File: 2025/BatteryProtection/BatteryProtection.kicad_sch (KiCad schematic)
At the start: 47 parts, among them J1 Conn_01x02_Socket, J2 Conn_01x02_Pin, J3 Conn_01x02_Pin, Q1 IXTA140P05T, Q10 BC847, Q11 BC847, Q12 BC847, Q2 BC847, Q3 BC847, Q4 BC847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

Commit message: Made a complete PCB design
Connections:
- net GPIO: now also J1.1 (Pin_1); no longer J3.1 (Pin_1)
- net VOUT: now also J3.1 (Pin_1); no longer J1.1 (Pin_1)
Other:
- moved on the sheet: J1
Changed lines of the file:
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@@
 	(wire
 		(pts
-			(xy 238.76 57.15) (xy 241.3 57.15)
-		)
-		(stroke
-			(width 0)
-			(type default)
-		)
-	)
-	(wire
-		(pts
 			(xy 39.37 175.26) (xy 41.91 175.26)
 		)
@@
 	(wire
 		(pts
-			(xy 257.81 90.17) (xy 262.89 90.17)
+			(xy 251.46 59.69) (xy 255.27 59.69)
 		)
 		(stroke
@@
 	(wire
 		(pts
-			(xy 238.76 59.69) (xy 241.3 59.69)
+			(xy 265.43 135.89) (xy 267.97 135.89)
 		)
 		(stroke
@@
 	(wire
 		(pts
-			(xy 265.43 135.89) (xy 267.97 135.89)
+			(xy 251.46 148.59) (xy 251.46 149.86)
 		)
 		(stroke
@@
 	(wire
 		(pts
-			(xy 251.46 148.59) (xy 251.46 149.86)
+			(xy 251.46 57.15) (xy 255.27 57.15)
 		)
 		(stroke
@@
 	(wire
 		(pts
-			(xy 238.76 62.23) (xy 238.76 59.69)
+			(xy 251.46 62.23) (xy 251.46 59.69)
 		)
 		(stroke
@@
 	(wire
 		(pts
-			(xy 260.35 92.71) (xy 257.81 92.71)
+			(xy 264.16 92.71) (xy 257.81 92.71)
 		)
 		(stroke
@@
 	(wire
 		(pts
-			(xy 260.35 95.25) (xy 260.35 92.71)
+			(xy 264.16 95.25) (xy 264.16 92.71)
 		)
 		(stroke
@@
 	(wire
 		(pts
+			(xy 251.46 53.34) (xy 251.46 57.15)
+		)
+		(stroke
+			(width 0)
+			(type default)
+		)
+	)
+	(wire
+		(pts
 			(xy 85.09 134.62) (xy 86.36 134.62)
 		)
@@
 	(wire
 		(pts
+			(xy 264.16 90.17) (xy 264.16 87.63)
+		)
+		(stroke
+			(width 0)
+			(type default)
+		)
+	)
+	(wire
+		(pts
 			(xy 110.49 64.77) (xy 116.84 64.77)
 		)
@@
 	(wire
 		(pts
-			(xy 238.76 54.61) (xy 238.76 57.15)
-		)
-		(stroke
-			(width 0)
-			(type default)
-		)
-	)
-	(wire
-		(pts
 			(xy 85.09 97.79) (xy 85.09 105.41)
 		)
@@
 	(wire
 		(pts
+			(xy 257.81 90.17) (xy 264.16 90.17)
+		)
+		(stroke
+			(width 0)
+			(type default)
+		)
+	)
+	(wire
+		(pts
 			(xy 124.46 167.64) (xy 124.46 189.23)
 		)
@@
 	(global_label "GPIO"
 		(shape input)
-		(at 262.89 90.17 0)
+		(at 251.46 53.34 180)
 		(fields_autoplaced yes)
 		(effects
@@
 				(size 1.27 1.27)
 			)
-			(justify left)
+			(justify right)
 		)
 		(property "Intersheetrefs" "${INTERSHEET_REFS}"
-			(at 270.3505 90.17 0)
+			(at 243.9995 53.34 0)
 			(effects
 				(font
 					(size 1.27 1.27)
 				)
-				(justify left)
+				(justify right)
 				(hide yes)
 			)
@@
 	(symbol
 		(lib_id "power:GND")
-		(at 238.76 62.23 0)
+		(at 251.46 62.23 0)
 		(unit 1)
 		(exclude_from_sim no)
@@
 		(fields_autoplaced yes)
 		(property "Reference" "#PWR027"
-			(at 238.76 68.58 0)
+			(at 251.46 68.58 0)
 			(effects
 				(font
@@
 		)
 		(property "Value" "GND"
-			(at 238.76 67.31 0)
+			(at 251.46 67.31 0)
 			(effects
 				(font
@@
 		)
 		(property "Footprint" ""
-			(at 238.76 62.23 0)
+			(at 251.46 62.23 0)
 			(effects
 				(font
@@
 		)
 		(property "Datasheet" ""
-			(at 238.76 62.23 0)
+			(at 251.46 62.23 0)
 			(effects
 				(font
@@
 		)
 		(property "Description" "Power symbol creates a global label with name \"GND\" , ground"
-			(at 238.76 62.23 0)
+			(at 251.46 62.23 0)
 			(effects
 				(font
@@
 	(symbol
 		(lib_id "power:GND")
-		(at 260.35 95.25 0)
+		(at 264.16 95.25 0)
 		(unit 1)
 		(exclude_from_sim no)
@@
 		(fields_autoplaced yes)
 		(property "Reference" "#PWR032"
-			(at 260.35 101.6 0)
+			(at 264.16 101.6 0)
 			(effects
 				(font
@@
 		)
 		(property "Value" "GND"
-			(at 260.35 100.33 0)
+			(at 264.16 100.33 0)
 			(effects
 				(font
@@
 		)
 		(property "Footprint" ""
-			(at 260.35 95.25 0)
+			(at 264.16 95.25 0)
 			(effects
 				(font
@@
 		)
 		(property "Datasheet" ""
-			(at 260.35 95.25 0)
+			(at 264.16 95.25 0)
 			(effects
 				(font
@@
 		)
 		(property "Description" "Power symbol creates a global label with name \"GND\" , ground"
-			(at 260.35 95.25 0)
+			(at 264.16 95.25 0)
 			(effects
 				(font
@@
 	(symbol
 		(lib_id "Connector:Conn_01x02_Socket")
-		(at 246.38 57.15 0)
+		(at 260.35 57.15 0)
 		(unit 1)
 		(exclude_from_sim no)
@@
 		(fields_autoplaced yes)
 		(property "Reference" "J1"
-			(at 247.65 57.1499 0)
+			(at 261.62 57.1499 0)
 			(effects
 				(font
@@
 		)
 		(property "Value" "Conn_01x02_Socket"
-			(at 247.65 59.6899 0)
+			(at 261.62 59.6899 0)
 			(effects
 				(font
@@
 		)
 		(property "Footprint" "Connector_JST:JST_XH_B2B-XH-A_1x02_P2.50mm_Vertical"
-			(at 246.38 57.15 0)
+			(at 260.35 57.15 0)
 			(effects
 				(font
@@
 		)
 		(property "Datasheet" "~"
-			(at 246.38 57.15 0)
+			(at 260.35 57.15 0)
 			(effects
 				(font
@@
 		)
 		(property "Description" "Generic connector, single row, 01x02, script generated"
-			(at 246.38 57.15 0)
+			(at 260.35 57.15 0)
 			(effects
 				(font
@@
 	(symbol
 		(lib_id "power:+3.3V")
-		(at 238.76 54.61 0)
+		(at 264.16 87.63 0)
 		(unit 1)
 		(exclude_from_sim no)
@@
 		(dnp no)
 		(property "Reference" "#PWR030"
-			(at 238.76 58.42 0)
+			(at 264.16 91.44 0)
 			(effects
 				(font
@@
 		)
 		(property "Value" "VOUT"
-			(at 238.76 50.8 0)
+			(at 264.16 83.82 0)
 			(effects
 				(font
@@
 		)
 		(property "Footprint" ""
-			(at 238.76 54.61 0)
+			(at 264.16 87.63 0)
 			(effects
 				(font
@@
 		)
 		(property "Datasheet" ""
-			(at 238.76 54.61 0)
+			(at 264.16 87.63 0)
 			(effects
 				(font
@@
 		)
 		(property "Description" "Power symbol creates a global label with name \"+3.3V\""
-			(at 238.76 54.61 0)
+			(at 264.16 87.63 0)
 			(effects
 				(font

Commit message: more work on PCB
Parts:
- added D1: LED, LED_SMD:LED_0805_2012Metric, symbol Device:LED
- added R26: 2.2k, Resistor_SMD:R_0603_1608Metric_Pad0.98x0.95mm_HandSolder, symbol Device:R_US
- added TP1: GPIO, TestPoint:TestPoint_Pad_D1.5mm, symbol Connector:TestPoint
- added TP2, TP7: Vout, TestPoint:TestPoint_Pad_D1.5mm, symbol Connector:TestPoint
- added TP3: Vin, TestPoint:TestPoint_Pad_D1.5mm, symbol Connector:TestPoint
- added TP4: U1 Out, TestPoint:TestPoint_Pad_D1.5mm, symbol Connector:TestPoint
- added TP5: U2 Out, TestPoint:TestPoint_Pad_D1.5mm, symbol Connector:TestPoint
- added TP6: Kill, TestPoint:TestPoint_Pad_D1.5mm, symbol Connector:TestPoint
- added TP8: Pmos In, TestPoint:TestPoint_Pad_D1.5mm, symbol Connector:TestPoint
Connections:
- net GND: now also R26.1
- net GPIO: now also TP1.1
- net VOUT: now also TP2.1
- net Vs: now also TP3.1
- net at R6.1, U2.1: now also TP5.1
- net at Q9.3 (C), R17.1, R18.1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: now also TP7.1
- net at Q1.1 (G), Q12.3 (C), R9.1: now also TP8.1
- net at Q8.3 (C), R13.1, R7.1: now also D1.2 (A), TP6.1
- net at R5.2, U1.1: now also TP4.1
- new net: D1.1 (K), R26.2

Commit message: DID the voltage protection PCB
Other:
- note removed: "Change transistors to this one"
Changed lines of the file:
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@@
-		)
-	)
-	(text "Change transistors to this one"
-		(exclude_from_sim no)
-		(at 182.88 144.78 0)
-		(effects
-			(font
-				(size 2.54 2.54)
-				(thickness 0.508)
-				(bold yes)
-			)
 		)
 	)

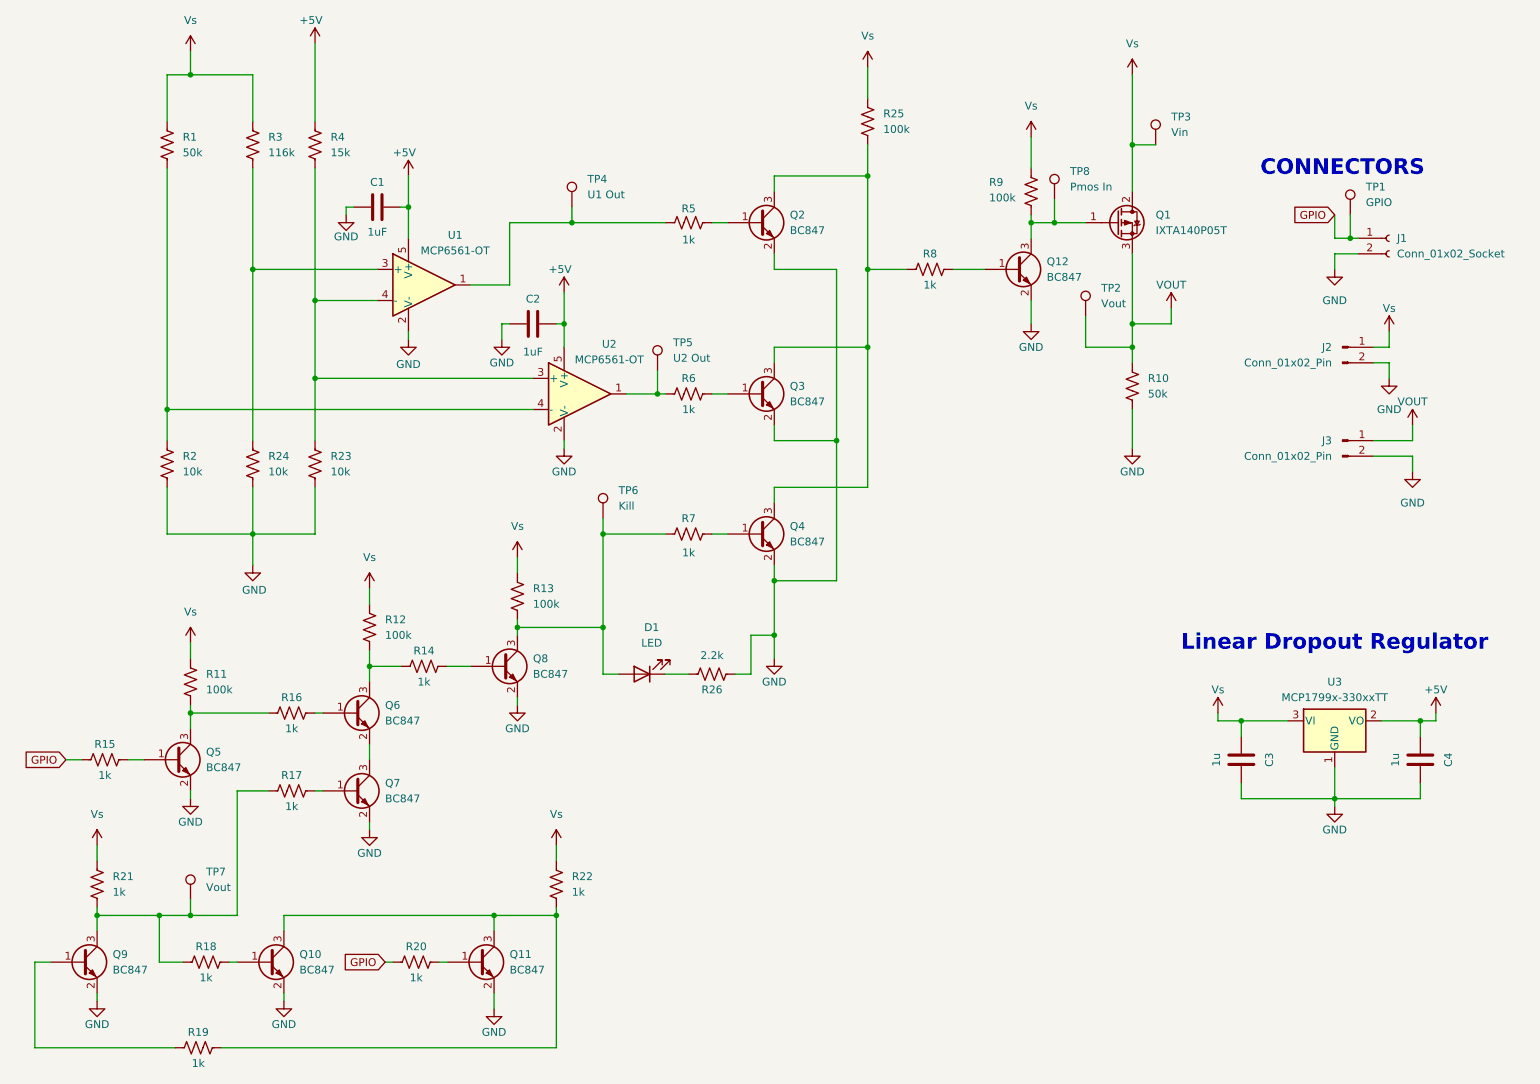
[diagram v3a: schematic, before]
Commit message: Added Switch to Bat Protect Board
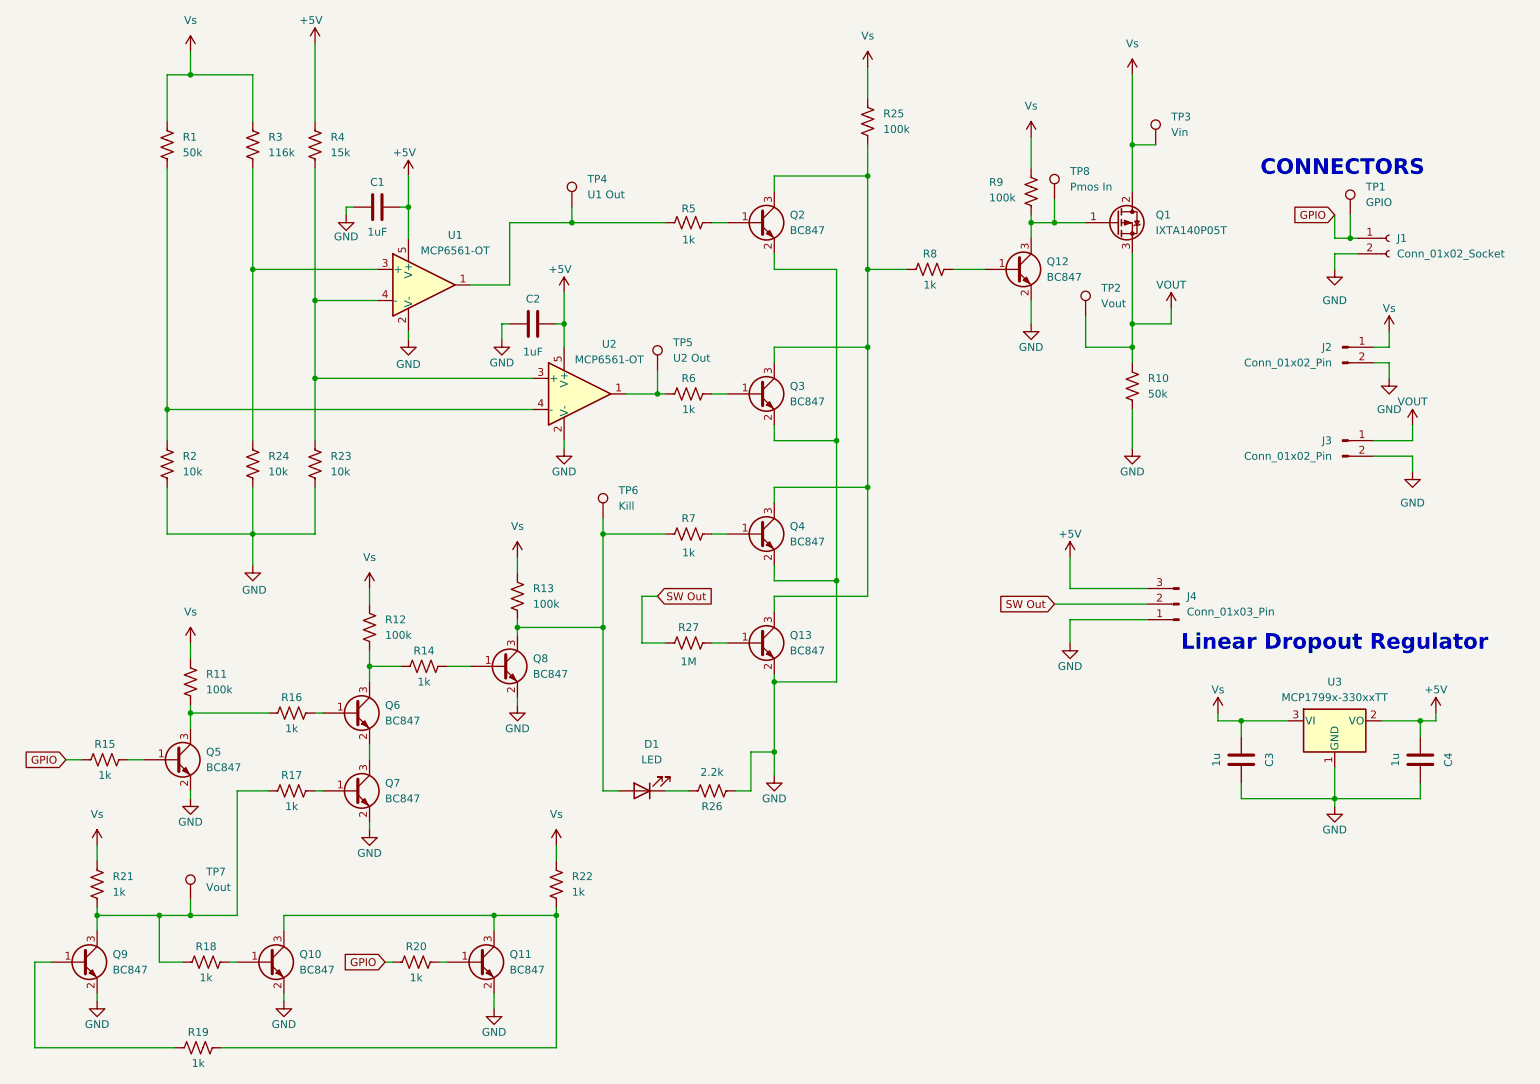
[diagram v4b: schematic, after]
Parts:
- added J4: Conn_01x03_Pin, B3B-XH-A:JST_B3B-XH-A, symbol Connector:Conn_01x03_Pin
- added Q13: BC847, Package_TO_SOT_SMD:SOT-23, symbol Transistor_BJT:BC847
- added R27: 1M, Resistor_SMD:R_0603_1608Metric_Pad0.98x0.95mm_HandSolder, symbol Device:R_US
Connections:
- net +5V: now also J4.3 (Pin_3)
- net GND: now also J4.1 (Pin_1), Q13.2 (E)
- net at Q2.3 (C), Q3.3 (C), Q4.3 (C)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: now also Q13.3 (C)
- new net: Q13.1 (B), R27.2
- new net SW Out: J4.2 (Pin_2), R27.1
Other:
- moved on the sheet: D1, R26
